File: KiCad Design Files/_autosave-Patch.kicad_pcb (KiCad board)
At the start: 2 copper layers, 47 x 47 mm, 5 parts, among them J1 RF Connector

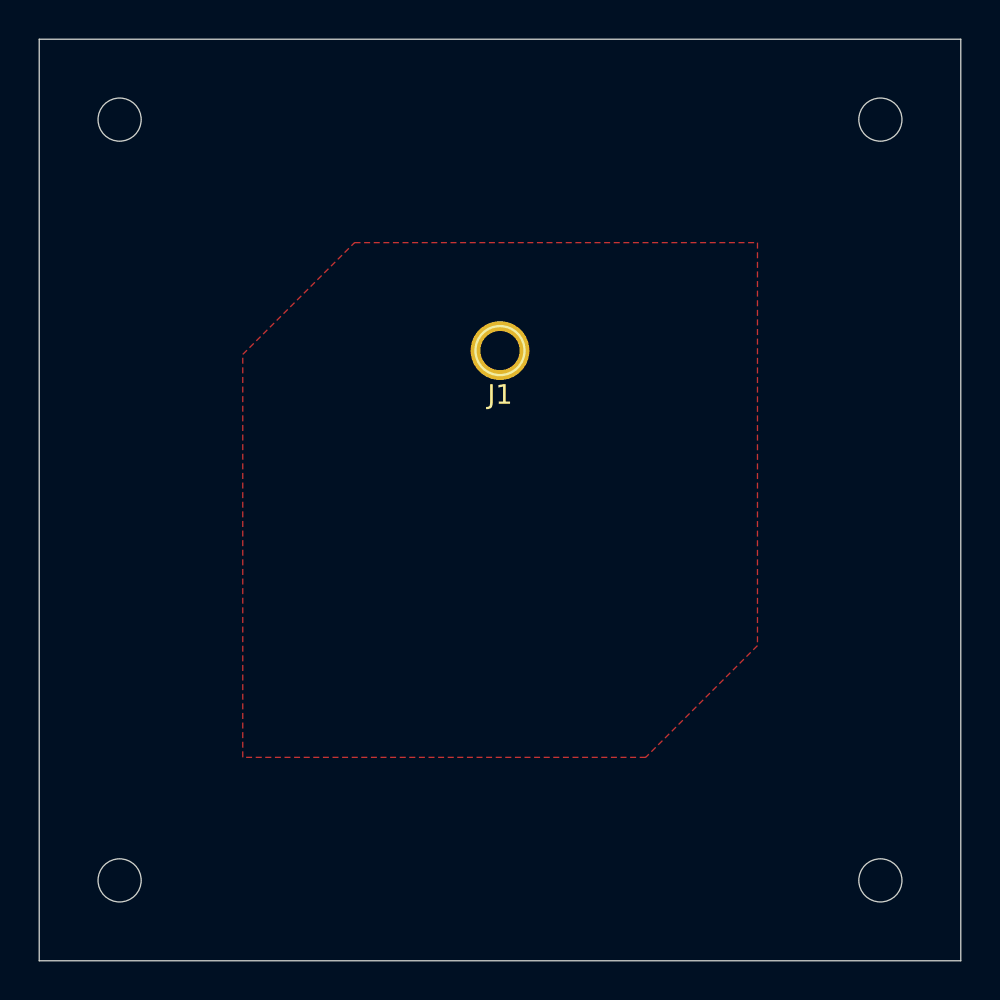
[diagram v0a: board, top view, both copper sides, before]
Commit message: Added mounting holes+top pads+bot GND pad
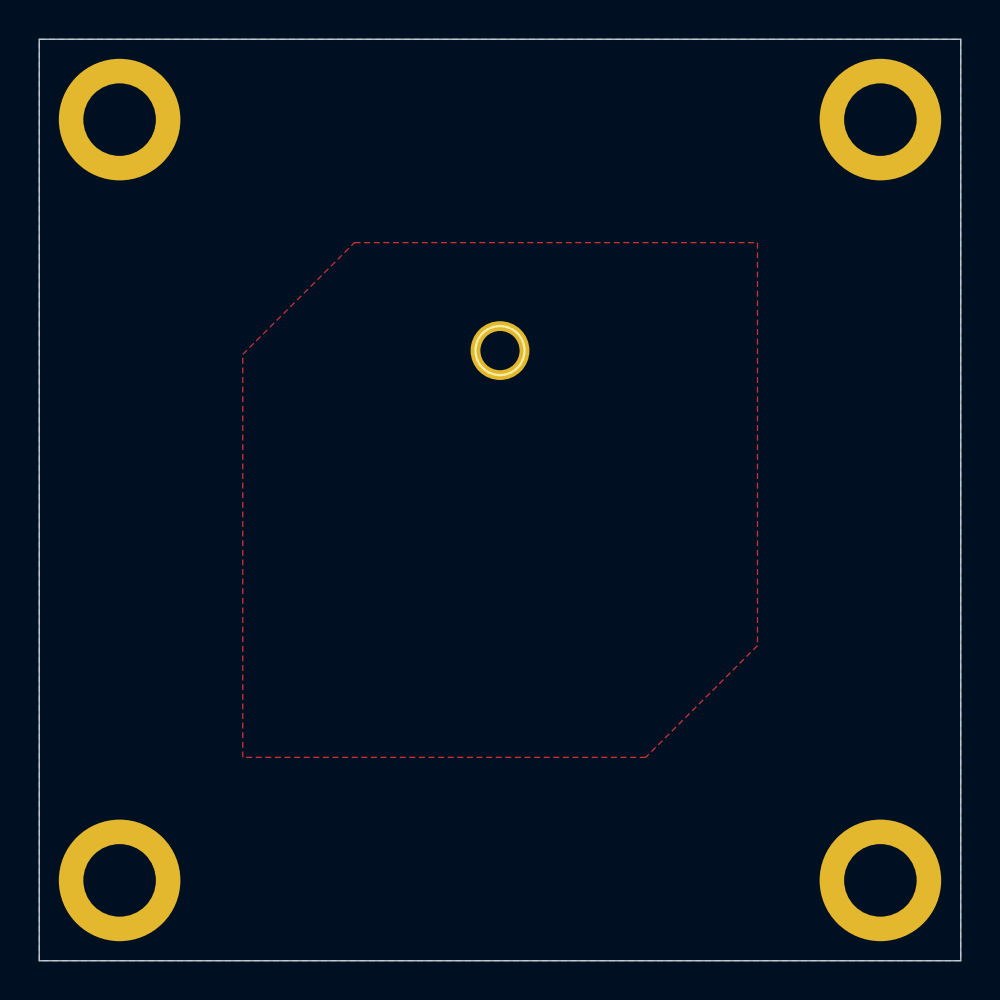
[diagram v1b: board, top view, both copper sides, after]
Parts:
- removed the REF** at (118.2, 76.9)
- removed the REF** at (118.2, 38.1)
- removed the REF** at (79.4, 76.9)
- removed the REF** at (79.4, 38.1)
- added REF**: MountingHole_3.7mm_Pad, MountingHole:MountingHole_3.7mm_Pad, F.Cu at (118.2, 76.9)
- added REF**: MountingHole_3.7mm_Pad, MountingHole:MountingHole_3.7mm_Pad, F.Cu at (79.4, 76.9)
- added REF**: MountingHole_3.7mm_Pad, MountingHole:MountingHole_3.7mm_Pad, F.Cu at (118.2, 38.1)
- added REF**: MountingHole_3.7mm_Pad, MountingHole:MountingHole_3.7mm_Pad, F.Cu at (79.4, 38.1)
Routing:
- added copper zone on B.Cu, net (none)
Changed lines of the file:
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@@
 (kicad_pcb (version 20171130) (host pcbnew "(5.1.10)-1")
   (general
-    (thickness 1.6)
-    (drawings 4)
+    (thickness 4.5)
+    (drawings 5)
     (tracks 0)
     (zones 0)
@@
     (mod_text_size 1 1)
     (mod_text_width 0.15)
-    (pad_size 2.2 2.2)
-    (pad_drill 2.2)
+    (pad_size 6.2 6.2)
+    (pad_drill 3.7)
     (pad_to_mask_clearance 0.05)
     (aux_axis_origin 0 0)
@@
     (add_net /RF_COPPER)
   )
-  (module MountingHole:MountingHole_2.2mm_M2 (layer Top)
+  (module MountingHole:MountingHole_3.7mm_Pad (layer Top)
     (at 118.2187 76.8802)
-    (descr "Mounting Hole 2.2mm, no annular, M2")
-    (tags "mounting hole 2.2mm no annular m2")
-    (attr virtual)
-    (fp_text reference REF** (at 0 -3.2) (layer F.SilkS) hide
-      (effects (font (size 1 1) (thickness 0.15)))
-    )
-    (fp_text value MountingHole_2.2mm_M2 (at 0 3.2) (layer F.Fab)
-      (effects (font (size 1 1) (thickness 0.15)))
-    )
-    (fp_circle (center 0 0) (end 2.45 0) (layer F.CrtYd) (width 0.05))
-    (fp_circle (center 0 0) (end 2.2 0) (layer Cmts.User) (width 0.15))
-    (fp_text user %R (at 0.3 0) (layer F.Fab)
-      (effects (font (size 1 1) (thickness 0.15)))
-    )
-    (pad "" np_thru_hole circle (at 0 0) (size 2.2 2.2) (drill 2.2) (layers *.Cu *.Mask)
-      (clearance 0.5))
-  )
-  (module MountingHole:MountingHole_2.2mm_M2 (layer Top)
+    (descr "Mounting Hole 3.7mm")
+    (tags "mounting hole 3.7mm")
+    (attr virtual)
+    (fp_text reference REF** (at 0 -4.7) (layer F.SilkS) hide
+      (effects (font (size 1 1) (thickness 0.15)))
+    )
+    (fp_text value MountingHole_3.7mm_Pad (at 0 4.7) (layer F.Fab)
+      (effects (font (size 1 1) (thickness 0.15)))
+    )
+    (fp_circle (center 0 0) (end 3.7 0) (layer Cmts.User) (width 0.15))
+    (fp_circle (center 0 0) (end 3.95 0) (layer F.CrtYd) (width 0.05))
+    (fp_text user %R (at 0.3 0) (layer F.Fab)
+      (effects (font (size 1 1) (thickness 0.15)))
+    )
+    (pad 1 thru_hole circle (at 0 0) (size 6.2 6.2) (drill 3.7) (layers Top F.Mask))
+  )
+  (module MountingHole:MountingHole_3.7mm_Pad (layer Top)
+    (at 79.4187 76.8802)
+    (descr "Mounting Hole 3.7mm")
+    (tags "mounting hole 3.7mm")
+    (attr virtual)
+    (fp_text reference REF** (at 0 -4.7) (layer F.SilkS) hide
+      (effects (font (size 1 1) (thickness 0.15)))
+    )
+    (fp_text value MountingHole_3.7mm_Pad (at 0 4.7) (layer F.Fab)
+      (effects (font (size 1 1) (thickness 0.15)))
+    )
+    (fp_circle (center 0 0) (end 3.7 0) (layer Cmts.User) (width 0.15))
+    (fp_circle (center 0 0) (end 3.95 0) (layer F.CrtYd) (width 0.05))
+    (fp_text user %R (at 0.3 0) (layer F.Fab)
+      (effects (font (size 1 1) (thickness 0.15)))
+    )
+    (pad 1 thru_hole circle (at 0 0) (size 6.2 6.2) (drill 3.7) (layers Top F.Mask))
+  )
+  (module MountingHole:MountingHole_3.7mm_Pad (layer Top)
     (at 118.2187 38.0802)
-    (descr "Mounting Hole 2.2mm, no annular, M2")
-    (tags "mounting hole 2.2mm no annular m2")
-    (attr virtual)
-    (fp_text reference REF** (at 0 -3.2) (layer F.SilkS) hide
-      (effects (font (size 1 1) (thickness 0.15)))
-    )
-    (fp_text value MountingHole_2.2mm_M2 (at 0 3.2) (layer F.Fab)
-      (effects (font (size 1 1) (thickness 0.15)))
-    )
-    (fp_circle (center 0 0) (end 2.45 0) (layer F.CrtYd) (width 0.05))
-    (fp_circle (center 0 0) (end 2.2 0) (layer Cmts.User) (width 0.15))
-    (fp_text user %R (at 0.3 0) (layer F.Fab)
-      (effects (font (size 1 1) (thickness 0.15)))
-    )
-    (pad "" np_thru_hole circle (at 0 0) (size 2.2 2.2) (drill 2.2) (layers *.Cu *.Mask)
-      (clearance 0.5))
-  )
-  (module MountingHole:MountingHole_2.2mm_M2 (layer Top)
-    (at 79.4187 76.8802)
-    (descr "Mounting Hole 2.2mm, no annular, M2")
-    (tags "mounting hole 2.2mm no annular m2")
-    (attr virtual)
-    (fp_text reference REF** (at 0 -3.2) (layer F.SilkS) hide
-      (effects (font (size 1 1) (thickness 0.15)))
-    )
-    (fp_text value MountingHole_2.2mm_M2 (at 0 3.2) (layer F.Fab)
-      (effects (font (size 1 1) (thickness 0.15)))
-    )
-    (fp_circle (center 0 0) (end 2.45 0) (layer F.CrtYd) (width 0.05))
-    (fp_circle (center 0 0) (end 2.2 0) (layer Cmts.User) (width 0.15))
-    (fp_text user %R (at 0.3 0) (layer F.Fab)
-      (effects (font (size 1 1) (thickness 0.15)))
-    )
-    (pad "" np_thru_hole circle (at 0 0) (size 2.2 2.2) (drill 2.2) (layers *.Cu *.Mask)
-      (clearance 0.5))
-  )
-  (module MountingHole:MountingHole_2.2mm_M2 (layer Top)
+    (descr "Mounting Hole 3.7mm")
+    (tags "mounting hole 3.7mm")
+    (attr virtual)
+    (fp_text reference REF** (at 0 -4.7) (layer F.SilkS) hide
+      (effects (font (size 1 1) (thickness 0.15)))
+    )
+    (fp_text value MountingHole_3.7mm_Pad (at 0 4.7) (layer F.Fab)
+      (effects (font (size 1 1) (thickness 0.15)))
+    )
+    (fp_circle (center 0 0) (end 3.7 0) (layer Cmts.User) (width 0.15))
+    (fp_circle (center 0 0) (end 3.95 0) (layer F.CrtYd) (width 0.05))
+    (fp_text user %R (at 0.3 0) (layer F.Fab)
+      (effects (font (size 1 1) (thickness 0.15)))
+    )
+    (pad 1 thru_hole circle (at 0 0) (size 6.2 6.2) (drill 3.7) (layers Top F.Mask))
+  )
+  (module MountingHole:MountingHole_3.7mm_Pad (layer Top)
     (at 79.4187 38.0802)
-    (descr "Mounting Hole 2.2mm, no annular, M2")
-    (tags "mounting hole 2.2mm no annular m2")
-    (attr virtual)
-    (fp_text reference REF** (at 0 -3.2) (layer F.SilkS) hide
-      (effects (font (size 1 1) (thickness 0.15)))
-    )
-    (fp_text value MountingHole_2.2mm_M2 (at 0 3.2) (layer F.Fab)
-      (effects (font (size 1 1) (thickness 0.15)))
-    )
-    (fp_text user %R (at 0.3 0) (layer F.Fab)
-      (effects (font (size 1 1) (thickness 0.15)))
-    )
-    (fp_circle (center 0 0) (end 2.2 0) (layer Cmts.User) (width 0.15))
-    (fp_circle (center 0 0) (end 2.45 0) (layer F.CrtYd) (width 0.05))
-    (pad "" np_thru_hole circle (at 0 0) (size 2.2 2.2) (drill 2.2) (layers *.Cu *.Mask)
-      (clearance 0.5))
+    (descr "Mounting Hole 3.7mm")
+    (tags "mounting hole 3.7mm")
+    (attr virtual)
+    (fp_text reference REF** (at 0 -4.7) (layer F.SilkS) hide
+      (effects (font (size 1 1) (thickness 0.15)))
+    )
+    (fp_text value MountingHole_3.7mm_Pad (at 0 4.7) (layer F.Fab)
+      (effects (font (size 1 1) (thickness 0.15)))
+    )
+    (fp_text user %R (at 0.3 0) (layer F.Fab)
+      (effects (font (size 1 1) (thickness 0.15)))
+    )
+    (fp_circle (center 0 0) (end 3.7 0) (layer Cmts.User) (width 0.15))
+    (fp_circle (center 0 0) (end 3.95 0) (layer F.CrtYd) (width 0.05))
+    (pad 1 thru_hole circle (at 0 0) (size 6.2 6.2) (drill 3.7) (layers Top F.Mask))
   )
   (module Connector_Pin:Pin_D1.0mm_L10.0mm (layer Top)
@@
     (tags "solder Pin_ press fit")
     (clearance 1)
-    (fp_text reference J1 (at 0 2.25) (layer F.SilkS)
+    (fp_text reference J1 (at 0 2.25) (layer F.SilkS) hide
       (effects (font (size 1 1) (thickness 0.15)))
     )
@@
       (effects (font (size 1 1) (thickness 0.15)))
     )
+    (fp_circle (center 0 0) (end 1.5 0) (layer F.CrtYd) (width 0.05))
+    (fp_circle (center 0 0) (end 0.5 0) (layer F.Fab) (width 0.12))
+    (fp_circle (center 0 0) (end 1 0) (layer F.Fab) (width 0.12))
     (fp_circle (center 0 0) (end 1.25 0.05) (layer F.SilkS) (width 0.12))
-    (fp_circle (center 0 0) (end 1 0) (layer F.Fab) (width 0.12))
-    (fp_circle (center 0 0) (end 0.5 0) (layer F.Fab) (width 0.12))
-    (fp_circle (center 0 0) (end 1.5 0) (layer F.CrtYd) (width 0.05))
     (fp_text user %R (at 0 2.25) (layer F.Fab)
       (effects (font (size 1 1) (thickness 0.15)))
@@
     (pad 1 thru_hole circle (at 0 0) (size 3 3) (drill 2) (layers *.Cu *.Mask)
       (net 1 /RF_COPPER))
-    (model ${KISYS3DMOD}/Connector_Pin.3dshapes/Pin_D1.0mm_L10.0mm.wrl
-      (at (xyz 0 0 0))
-      (scale (xyz 1 1 1))
-      (rotate (xyz 0 0 0))
-    )
-  )
+  )
+  (gr_circle (center 98.806 49.8475) (end 102.793881 49.8475) (layer B.Mask) (width 2))
   (gr_line (start 122.3187 80.9802) (end 122.3187 33.9802) (layer Edge.Cuts) (width 0.001))
   (gr_line (start 122.3187 33.9802) (end 75.3187 33.9802) (layer Edge.Cuts) (width 0.001))
@@
       )
     )
+  )
+  (zone (net 0) (net_name "") (layer Bottom) (hatch edge 0.508)
+    (priority 6)
+    (connect_pads (clearance 0.000001))
+    (min_thickness 0.0254)
+    (fill yes (arc_segments 32) (thermal_gap 0.051) (thermal_bridge_width 0.051))
+    (polygon
+      (pts
+        (xy 122.3142 80.9757) (xy 75.3232 80.9757) (xy 75.3232 33.9847) (xy 122.3142 33.9847)
+      )
+    )
